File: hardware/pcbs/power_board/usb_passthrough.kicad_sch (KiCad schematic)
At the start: 3 parts, among them J3 USB3_B_Micro, J4 USB3_A

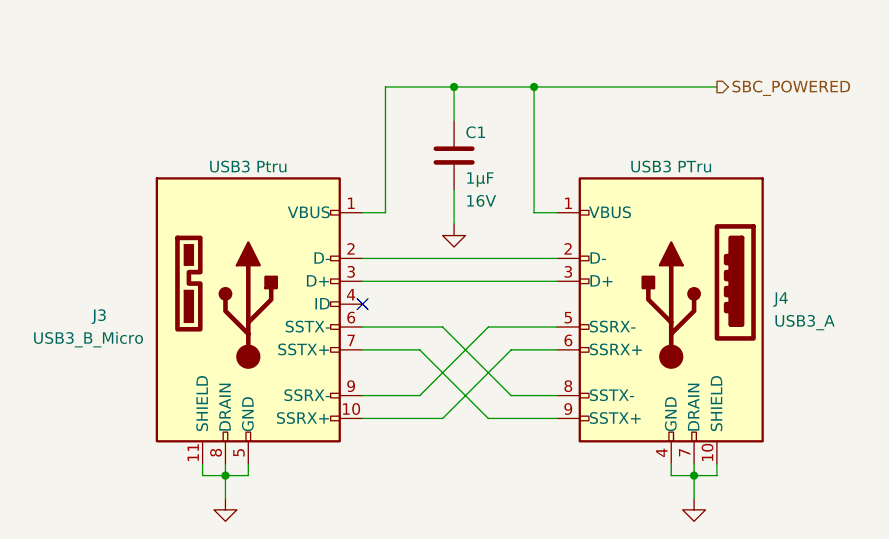
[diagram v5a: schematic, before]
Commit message: power_board: finalise isolated chargers and place USB3 passthrough
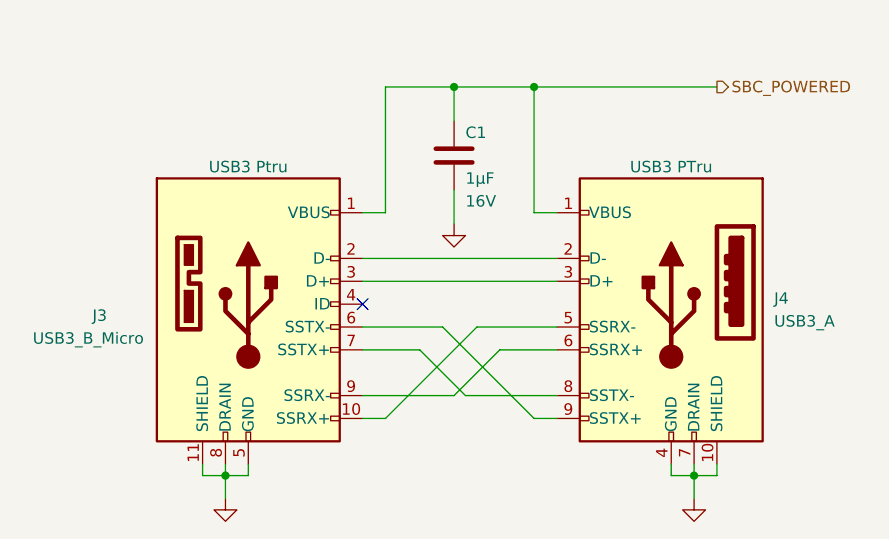
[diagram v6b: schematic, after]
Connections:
- net at J3.10 (SSRX+): now also J4.5 (SSRX-); no longer J4.6 (SSRX+)
- net at J3.6 (SSTX-): now also J4.9 (SSTX+); no longer J4.8 (SSTX-)
- net at J3.7 (SSTX+): now also J4.8 (SSTX-); no longer J4.9 (SSTX+)
- net at J3.9 (SSRX-): now also J4.6 (SSRX+); no longer J4.5 (SSRX-)
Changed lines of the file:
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@@
+	(wire
+		(pts
+			(xy 162.56 97.79) (xy 172.72 107.95)
+		)
+		(stroke
+			(width 0)
+			(type default)
+		)
+	)
+	(wire
+		(pts
+			(xy 153.67 105.41) (xy 163.83 105.41)
+		)
+		(stroke
+			(width 0)
+			(type default)
+		)
+	)
 	(wire
 		(pts
@@
 	(wire
 		(pts
+			(xy 153.67 100.33) (xy 160.02 100.33)
+		)
+		(stroke
+			(width 0)
+			(type default)
+		)
+	)
+	(wire
+		(pts
+			(xy 153.67 107.95) (xy 156.21 107.95)
+		)
+		(stroke
+			(width 0)
+			(type default)
+		)
+	)
+	(wire
+		(pts
 			(xy 163.83 82.55) (xy 163.83 86.36)
 		)
@@
 	(wire
 		(pts
-			(xy 170.18 105.41) (xy 162.56 97.79)
-		)
-		(stroke
-			(width 0)
-			(type default)
-		)
-	)
-	(wire
-		(pts
-			(xy 167.64 97.79) (xy 175.26 97.79)
+			(xy 165.1 105.41) (xy 160.02 100.33)
+		)
+		(stroke
+			(width 0)
+			(type default)
+		)
+	)
+	(wire
+		(pts
+			(xy 156.21 107.95) (xy 166.37 97.79)
+		)
+		(stroke
+			(width 0)
+			(type default)
+		)
+	)
+	(wire
+		(pts
+			(xy 166.37 97.79) (xy 175.26 97.79)
 		)
 		(stroke
@@
 	(wire
 		(pts
-			(xy 153.67 105.41) (xy 160.02 105.41)
-		)
-		(stroke
-			(width 0)
-			(type default)
-		)
-	)
-	(wire
-		(pts
 			(xy 153.67 85.09) (xy 156.21 85.09)
 		)
@@
 	(wire
 		(pts
-			(xy 153.67 107.95) (xy 162.56 107.95)
-		)
-		(stroke
-			(width 0)
-			(type default)
-		)
-	)
-	(wire
-		(pts
 			(xy 193.04 71.12) (xy 172.72 71.12)
 		)
@@
 	(wire
 		(pts
-			(xy 170.18 100.33) (xy 175.26 100.33)
+			(xy 168.91 100.33) (xy 175.26 100.33)
 		)
 		(stroke
@@
 	(wire
 		(pts
-			(xy 160.02 105.41) (xy 167.64 97.79)
-		)
-		(stroke
-			(width 0)
-			(type default)
-		)
-	)
-	(wire
-		(pts
 			(xy 163.83 71.12) (xy 163.83 74.93)
 		)
@@
 	(wire
 		(pts
-			(xy 170.18 100.33) (xy 162.56 107.95)
+			(xy 168.91 100.33) (xy 163.83 105.41)
 		)
 		(stroke
@@
 	(wire
 		(pts
-			(xy 153.67 100.33) (xy 160.02 100.33)
-		)
-		(stroke
-			(width 0)
-			(type default)
-		)
-	)
-	(wire
-		(pts
-			(xy 160.02 100.33) (xy 167.64 107.95)
-		)
-		(stroke
-			(width 0)
-			(type default)
-		)
-	)
-	(wire
-		(pts
-			(xy 167.64 107.95) (xy 175.26 107.95)
+			(xy 172.72 107.95) (xy 175.26 107.95)
 		)
 		(stroke
@@
 	(wire
 		(pts
-			(xy 170.18 105.41) (xy 175.26 105.41)
+			(xy 165.1 105.41) (xy 175.26 105.41)
 		)
 		(stroke
@@
 		(dnp no)
 		(fields_autoplaced yes)
-		(property "Reference" "#PWR07"
+		(property "Reference" "#PWR08"
 			(at 138.43 123.19 0)
 			(effects
@@
 			(project "power_board"
 				(path "/4b166175-80a4-48c6-994d-6e62a6160b87/91441b40-0438-4eff-8649-c295c7239fb6"
-					(reference "#PWR07")
+					(reference "#PWR08")
 					(unit 1)
 				)
@@
 		(dnp no)
 		(fields_autoplaced yes)
-		(property "Reference" "#PWR09"
+		(property "Reference" "#PWR010"
 			(at 190.5 123.19 0)
 			(effects
@@
 			(project "power_board"
 				(path "/4b166175-80a4-48c6-994d-6e62a6160b87/91441b40-0438-4eff-8649-c295c7239fb6"
-					(reference "#PWR09")
+					(reference "#PWR010")
 					(unit 1)
 				)
@@
 		(dnp no)
 		(fields_autoplaced yes)
-		(property "Reference" "#PWR08"
+		(property "Reference" "#PWR09"
 			(at 163.83 92.71 0)
 			(effects
@@
 			(project "power_board"
 				(path "/4b166175-80a4-48c6-994d-6e62a6160b87/91441b40-0438-4eff-8649-c295c7239fb6"
-					(reference "#PWR08")
+					(reference "#PWR09")
 					(unit 1)
 				)

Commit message: Re-route the usb3 differential pairs
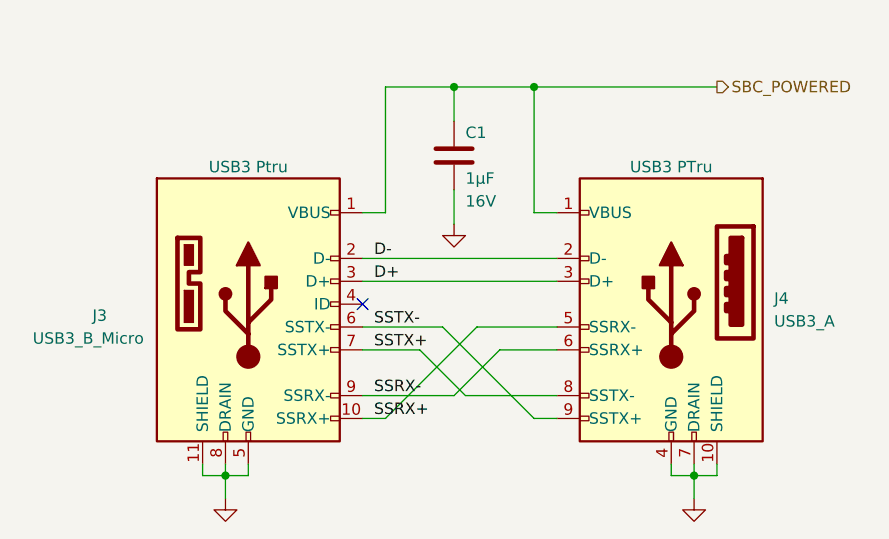
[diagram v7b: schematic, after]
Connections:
- net SSRX+: now reaches J3.10 (SSRX+), J4.5 (SSRX-)
- net D-: now reaches J3.2 (D-), J4.2 (D-)
- net D+: now reaches J3.3 (D+), J4.3 (D+)
- net SSTX-: now reaches J3.6 (SSTX-), J4.9 (SSTX+)
- net SSTX+: now reaches J3.7 (SSTX+), J4.8 (SSTX-)
- net SSRX-: now reaches J3.9 (SSRX-), J4.6 (SSRX+)
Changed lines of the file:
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@@
+		)
+	)
+	(label "D+"
+		(at 154.94 92.71 0)
+		(fields_autoplaced yes)
+		(effects
+			(font
+				(size 1.27 1.27)
+			)
+			(justify left bottom)
+		)
+	)
+	(label "D-"
+		(at 154.94 90.17 0)
+		(fields_autoplaced yes)
+		(effects
+			(font
+				(size 1.27 1.27)
+			)
+			(justify left bottom)
+		)
+	)
+	(label "SSTX+"
+		(at 154.94 100.33 0)
+		(fields_autoplaced yes)
+		(effects
+			(font
+				(size 1.27 1.27)
+			)
+			(justify left bottom)
+		)
+	)
+	(label "SSTX-"
+		(at 154.94 97.79 0)
+		(fields_autoplaced yes)
+		(effects
+			(font
+				(size 1.27 1.27)
+			)
+			(justify left bottom)
+		)
+	)
+	(label "SSRX-"
+		(at 154.94 105.41 0)
+		(fields_autoplaced yes)
+		(effects
+			(font
+				(size 1.27 1.27)
+			)
+			(justify left bottom)
+		)
+	)
+	(label "SSRX+"
+		(at 154.94 107.95 0)
+		(fields_autoplaced yes)
+		(effects
+			(font
+				(size 1.27 1.27)
+			)
+			(justify left bottom)
 		)
 	)

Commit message: power_board: final version
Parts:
- C1: LCSC (none) -> C28323
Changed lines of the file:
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@@
+			)
+		)
+		(property "LCSC" "C28323"
+			(at 163.83 78.74 0)
+			(effects
+				(font
+					(size 1.27 1.27)
+				)
+				(hide yes)
 			)
 		)
